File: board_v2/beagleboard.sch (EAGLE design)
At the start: 35 parts, among them U1 DWM1000, X1 5566-2, X2 04-JST-B4B-XH-A

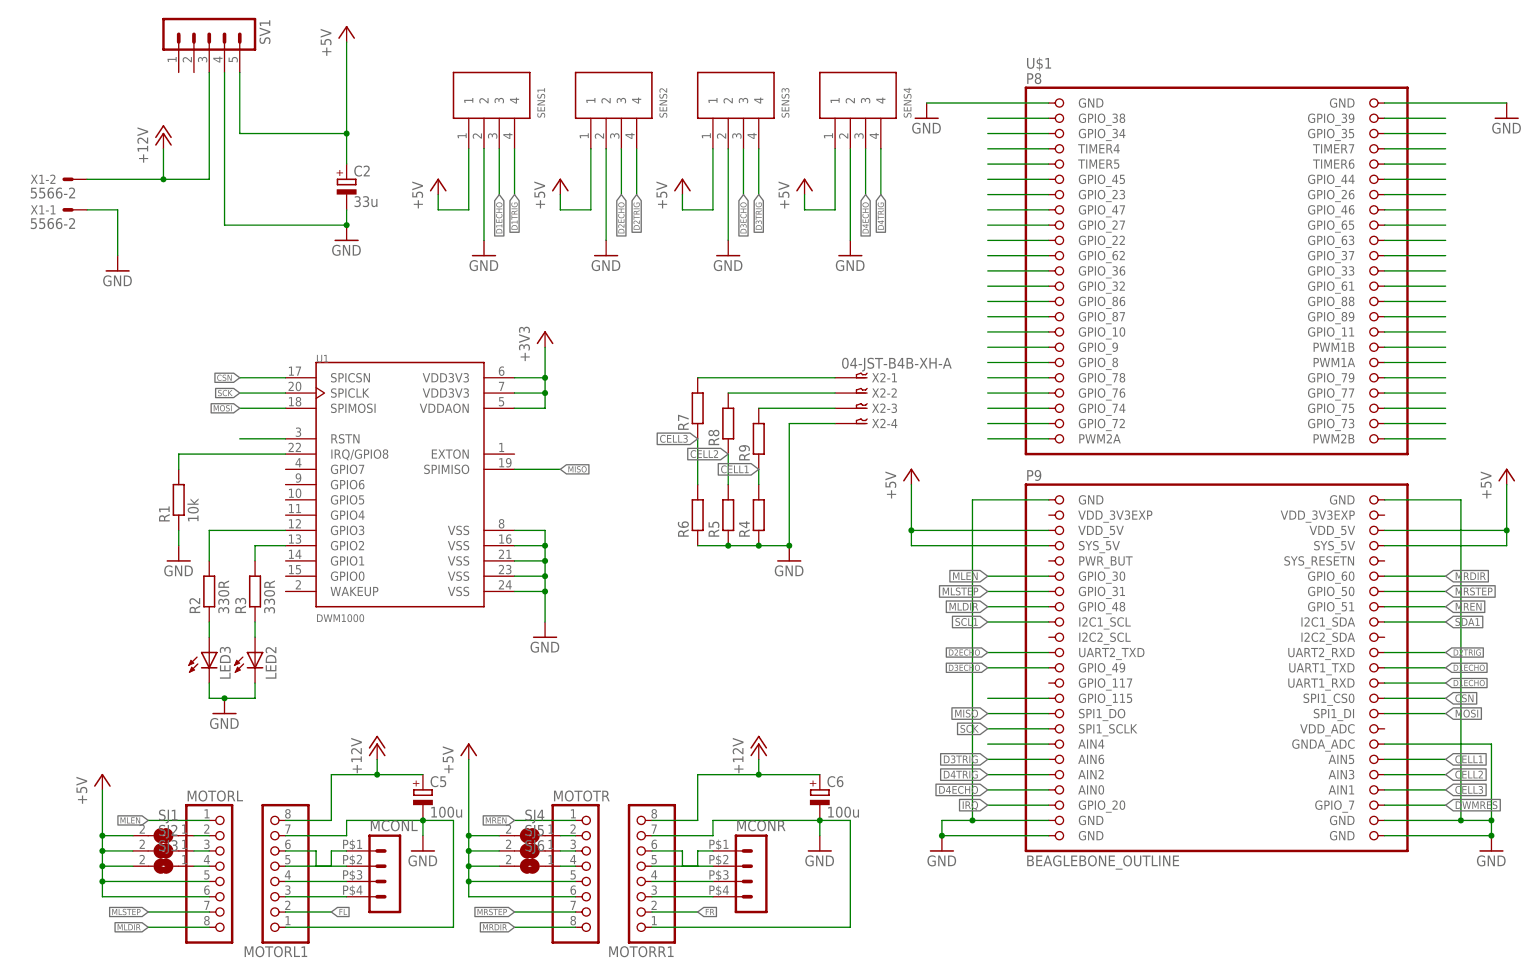
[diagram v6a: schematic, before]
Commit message: pin recinfiguration started
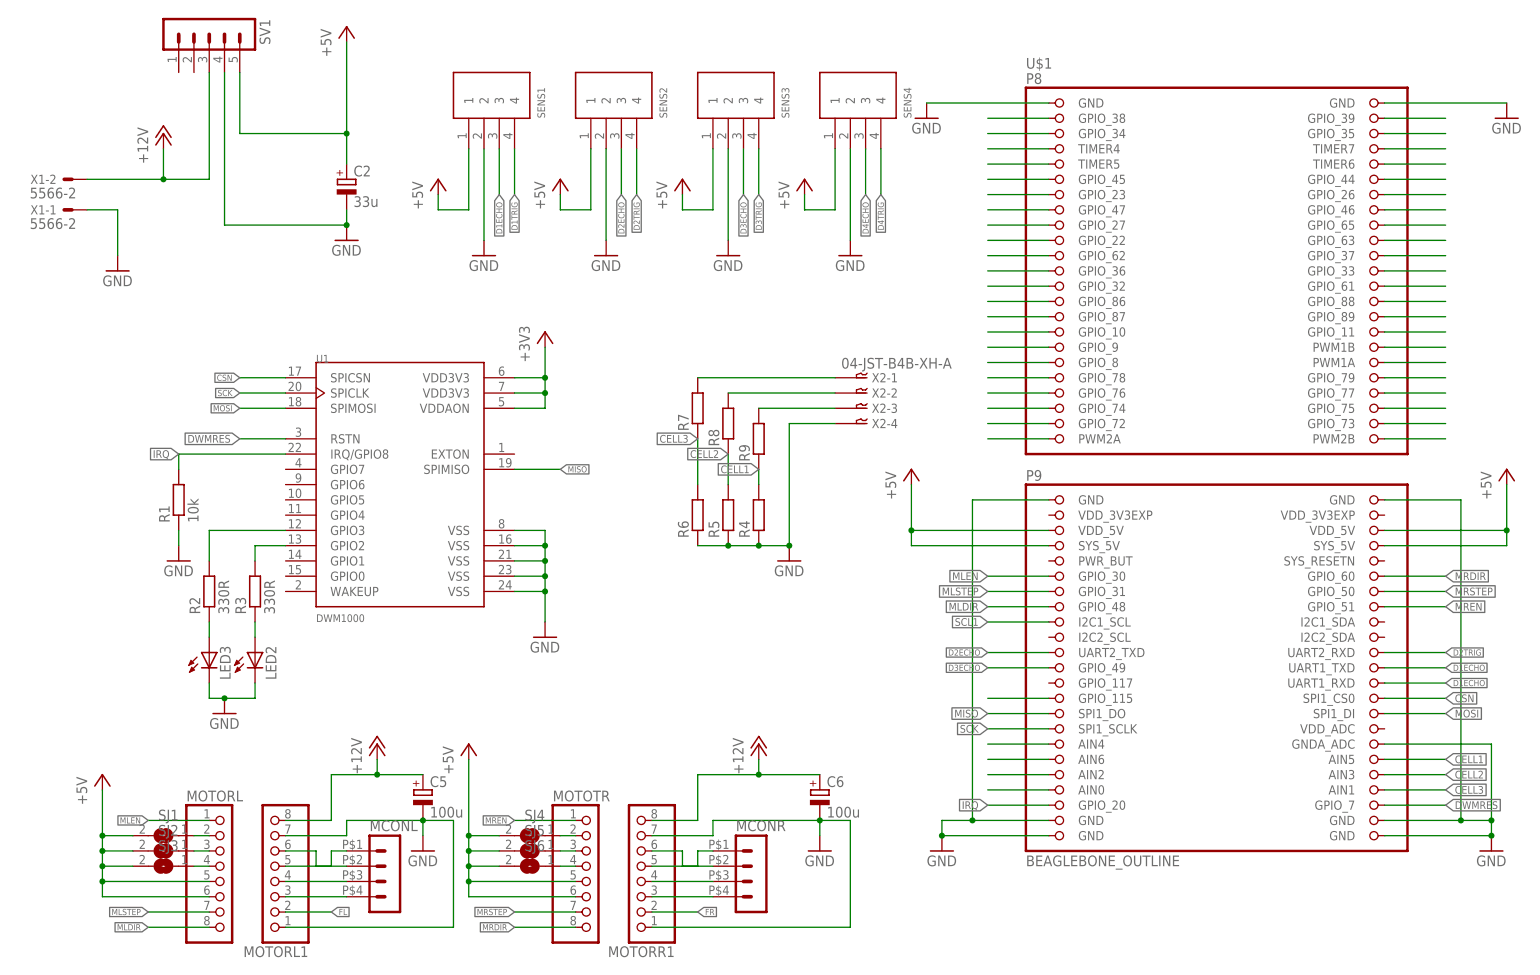
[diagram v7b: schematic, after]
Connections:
- removed net SDA1: U$1.I2C1_SDA
- new net N$67: U$1.AIN6
- net D3TRIG: no longer U$1.AIN6
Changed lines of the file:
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@@
 <pinref part="U1" gate="G$1" pin="RSTN"/>
 <wire x1="17.78" y1="63.5" x2="10.16" y2="63.5" width="0.1524" layer="91"/>
+<label x="10.16" y="63.5" size="1.27" layer="95" rot="R180" xref="yes"/>
 </segment>
 <segment>
@@
 <pinref part="R1" gate="G$1" pin="2"/>
 <wire x1="0" y1="60.96" x2="0" y2="58.42" width="0.1524" layer="91"/>
+<label x="0" y="60.96" size="1.27" layer="95" rot="R180" xref="yes"/>
 </segment>
 <segment>
@@
 <pinref part="U$1" gate="G$1" pin="AIN2"/>
 <wire x1="144.78" y1="7.62" x2="134.62" y2="7.62" width="0.1524" layer="91"/>
-<label x="134.62" y="7.62" size="1.27" layer="95" rot="R180" xref="yes"/>
 </segment>
 </net>
@@
 <pinref part="U$1" gate="G$1" pin="AIN0"/>
 <wire x1="144.78" y1="5.08" x2="134.62" y2="5.08" width="0.1524" layer="91"/>
-<label x="134.62" y="5.08" size="1.27" layer="95" rot="R180" xref="yes"/>
 </segment>
 </net>
@@
 <label x="96.52" y="104.14" size="1.016" layer="95" rot="R270" xref="yes"/>
 </segment>
-<segment>
-<pinref part="U$1" gate="G$1" pin="AIN6"/>
-<wire x1="144.78" y1="10.16" x2="134.62" y2="10.16" width="0.1524" layer="91"/>
-<label x="134.62" y="10.16" size="1.27" layer="95" rot="R180" xref="yes"/>
-</segment>
 </net>
 <net name="D3ECHO" class="0">
@@
 <pinref part="U$1" gate="G$1" pin="GND@2"/>
 <wire x1="200.66" y1="53.34" x2="213.36" y2="53.34" width="0.1524" layer="91"/>
-</segment>
-</net>
-<net name="SDA1" class="0">
-<segment>
-<pinref part="U$1" gate="G$1" pin="I2C1_SDA"/>
-<wire x1="200.66" y1="33.02" x2="210.82" y2="33.02" width="0.1524" layer="91"/>
-<label x="210.82" y="33.02" size="1.27" layer="95" xref="yes"/>
 </segment>
 </net>
@@
 </segment>
 </net>
+<net name="N$67" class="0">
+<segment>
+<pinref part="U$1" gate="G$1" pin="AIN6"/>
+<wire x1="144.78" y1="10.16" x2="134.62" y2="10.16" width="0.1524" layer="91"/>
+</segment>
+</net>

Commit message: new gpio routed started
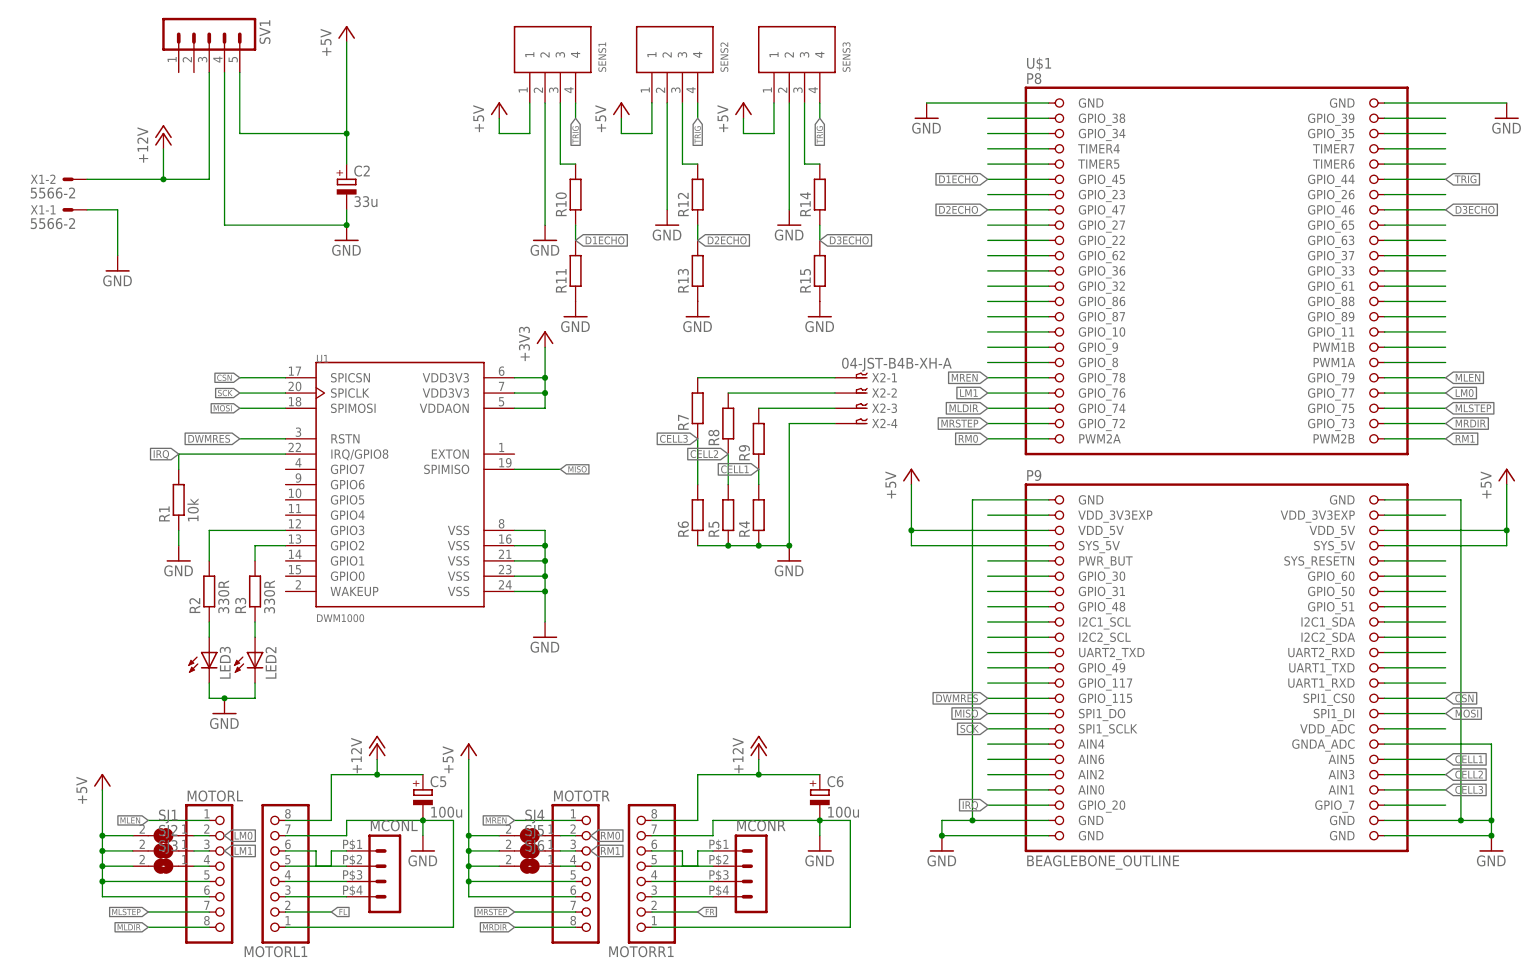
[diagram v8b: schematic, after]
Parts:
- removed SENS4: 4PIN, libsjst_eph:4PIN
- added R10, R11, R12, R13, R14, R15: (no value), rcl:R-EU_R0805
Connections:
- net SCL1 renamed N$79
- removed net D1TRIG: SENS1.4, U$1.UART1_RXD
- removed net D2TRIG: SENS2.4, U$1.UART2_RXD
- removed net D3TRIG: SENS3.4
- removed net N$101: U$1.GPIO_115
- removed net N$24: U$1.GPIO_44
- removed net N$26: U$1.GPIO_46
- removed net N$37: U$1.GPIO_79
- removed net N$38: U$1.GPIO_77
- removed net N$43: U$1.GPIO_45
- removed net N$45: U$1.GPIO_47
- new net LM0: MOTORL.2, SJ1.1, U$1.GPIO_77
- new net LM1: MOTORL.3, SJ2.1, U$1.GPIO_76
- new net N$68: U$1.I2C1_SDA
- new net N$69: U$1.I2C2_SDA
- new net N$70: U$1.VDD_ADC
- new net N$71: U$1.UART2_RXD
- new net N$72: U$1.UART1_TXD
- new net N$73: U$1.UART1_RXD
- new net N$74: U$1.UART2_TXD
- new net N$75: U$1.GPIO_49
- new net N$76: R10.2, SENS1.3
- new net N$77: U$1.GPIO_7
- new net N$78: R12.2, SENS2.3
- new net N$80: R14.2, SENS3.3
- new net RM0: MOTOTR.2, SJ4.1, U$1.PWM2A
- new net RM1: MOTOTR.3, SJ5.1, U$1.PWM2B
- new net TRIG: SENS1.4, SENS2.4, SENS3.4, U$1.GPIO_44
- net +5V: no longer SENS4.1
- net D1ECHO: now also R10.1, R11.2, U$1.GPIO_45; no longer SENS1.3, U$1.UART1_TXD
- net D2ECHO: now also R12.1, R13.2, U$1.GPIO_47; no longer SENS2.3, U$1.UART2_TXD
- net D3ECHO: now also R14.1, R15.2, U$1.GPIO_46; no longer SENS3.3, U$1.GPIO_49
- net D4ECHO: no longer SENS4.3
- net D4TRIG: no longer SENS4.4
- net DWMRES: now also U$1.GPIO_115; no longer U$1.GPIO_7
- net GND: now also R11.1, R13.1, R15.1; no longer SENS4.2
- net MLDIR: now also U$1.GPIO_74; no longer U$1.GPIO_48
- net MLEN: now also U$1.GPIO_79; no longer U$1.GPIO_30
- net MLSTEP: now also U$1.GPIO_75; no longer U$1.GPIO_31
- net MRDIR: now also U$1.GPIO_73; no longer U$1.GPIO_60
- net MREN: now also U$1.GPIO_78; no longer U$1.GPIO_51
- net MRSTEP: now also U$1.GPIO_72; no longer U$1.GPIO_50
- net N$39: now also U$1.PWR_BUT; no longer U$1.GPIO_75
- net N$40: now also U$1.VDD_3V3EXP@1; no longer U$1.GPIO_73
- net N$41: now also U$1.GPIO_30; no longer U$1.PWM2B
- net N$53: now also U$1.GPIO_31; no longer MOTORL.3, SJ2.1
- net N$54: now also U$1.GPIO_48; no longer MOTORL.2, SJ1.1
- net N$55: now also U$1.GPIO_117; no longer MOTOTR.2, SJ4.1
- net N$60: now also U$1.I2C2_SCL; no longer U$1.GPIO_78
- net N$61: now also U$1.VDD_3V3EXP@2; no longer U$1.GPIO_76
- net N$62: now also U$1.SYS_RESETN; no longer U$1.GPIO_74
- net N$63: now also U$1.GPIO_60; no longer U$1.GPIO_72
- net N$64: now also U$1.GPIO_50; no longer U$1.PWM2A
- net N$65: now also U$1.GPIO_51; no longer MOTOTR.3, SJ5.1
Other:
- moved on the sheet: SENS1, SENS2, SENS3
